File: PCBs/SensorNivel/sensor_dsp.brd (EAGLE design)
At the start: 100 x 80 mm, 76 parts, among them IC1 LD117AS, IC2 DSPIC33FJ12GP202/SP, IC4 7805TV, IC5 ICL7660CPA, IC6 4069N, IC7 LM324N, IC8 LM324N, IC9 MAX481CPA

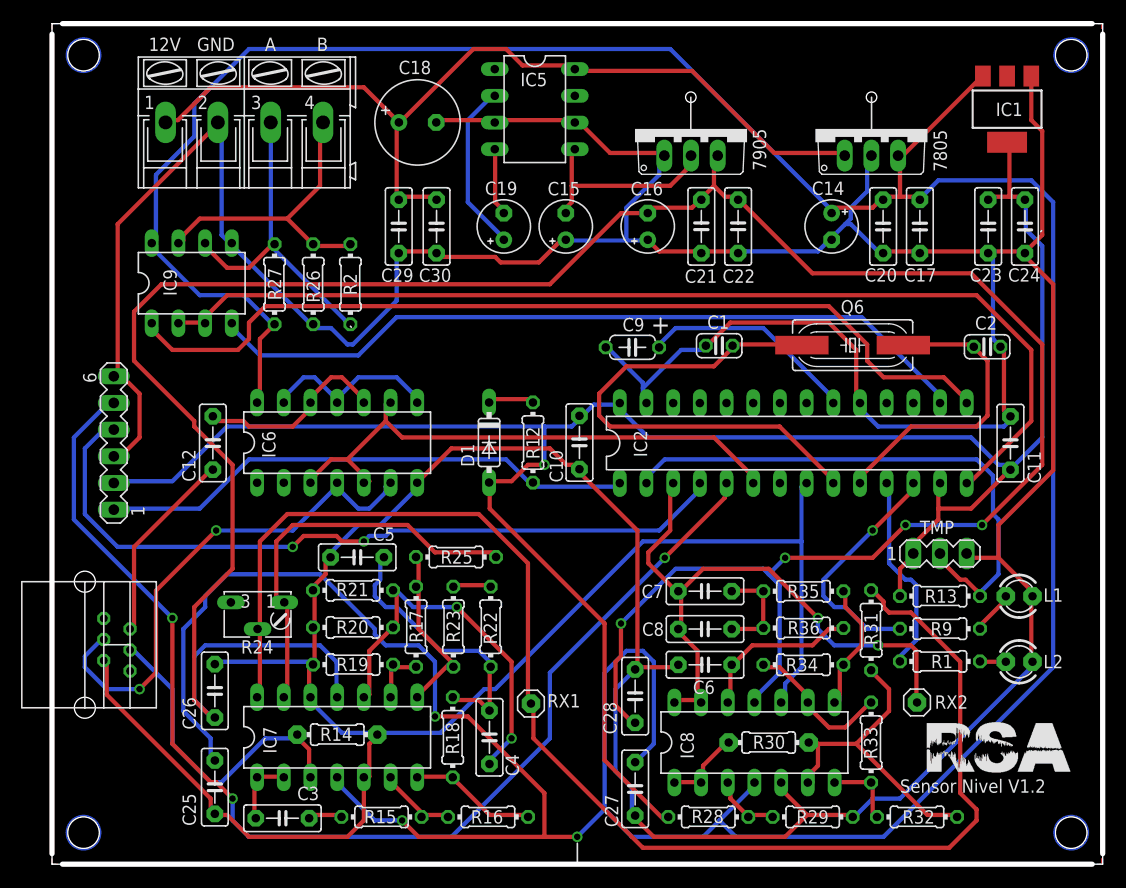
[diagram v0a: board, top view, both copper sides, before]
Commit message: Se rediseñaron y corrigieron los diseños de los PCB. Se diseñaron las platinas de los vertederos basadas en las medidas de los soportes.
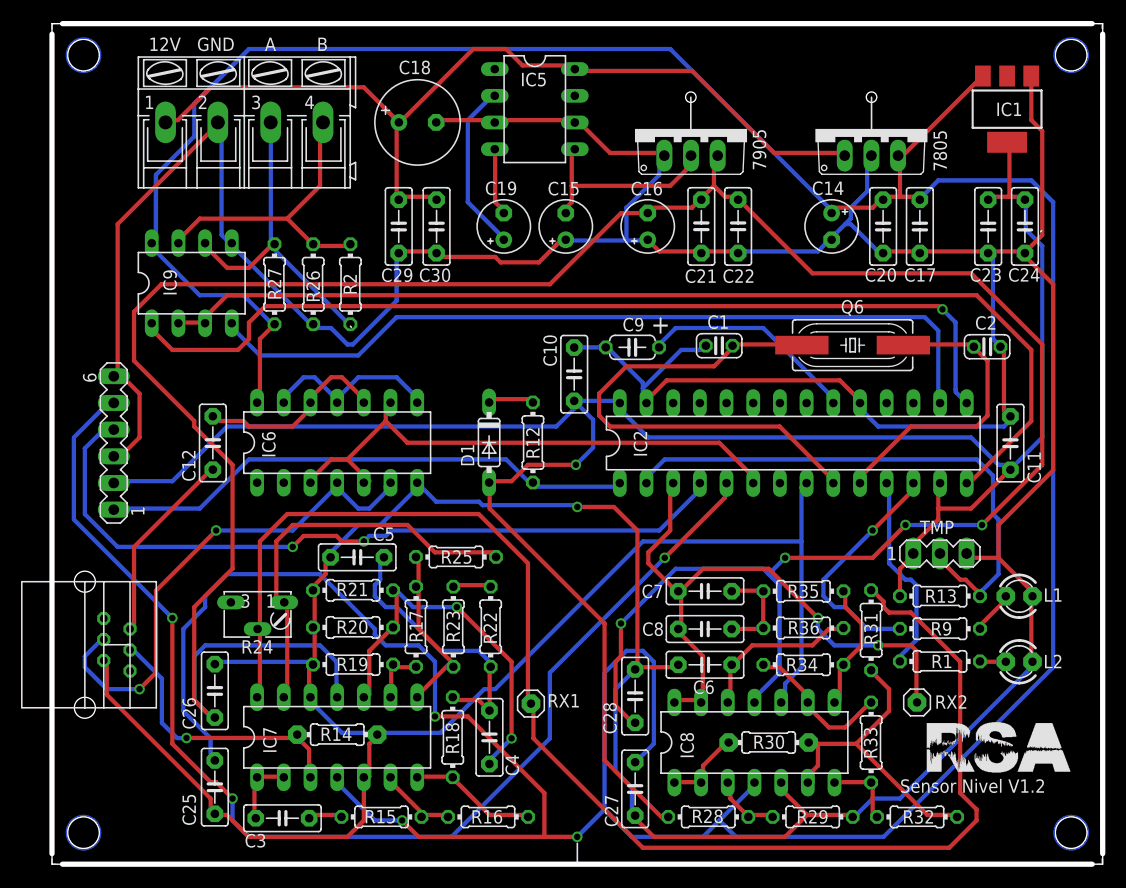
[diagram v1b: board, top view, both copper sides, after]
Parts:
- moved C10 6.52 mm to (49.7, 46.6), turned to 270 degrees
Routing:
- net VDD: track 198.1 -> 205.5 mm
- net R+: track 30.6 -> 26.6 mm, vias 0 -> 1
- net ERX: track 74.2 -> 77.7 mm
- net ETX: track 86.4 -> 89.3 mm, vias 0 -> 1
- net AGND: track 582.6 -> 583.8 mm, vias 0 -> 1
- net ADC_IN: track 59.0 -> 59.7 mm

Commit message: Se hicieron modificaciones al Firmware y al Software. Version funcional.
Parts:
- C1, C2: value (none) -> 22pF
- C10, C11, C12, C25, C26, C27, C28: value (none) -> 100nF
- C3, C4, C5: value (none) -> 10nF
- C6, C7, C8: value (none) -> 1nF
- C9: value (none) -> 10uF
- Q6: value (none) -> 8MHz
- R12, R13: value (none) -> 4.7K
- R14, R15, R20, R28, R29, R30, R31, R32, R33, R34: value (none) -> 10K
- R16: value (none) -> 1M
- R17, R25: value (none) -> 1K
- R18, R26, R27: value (none) -> 3.3K
- R19: value (none) -> 470
- R2: value (none) -> 120
- R21: value (none) -> 390
- R22, R23: value (none) -> 220
- R35, R36: value (none) -> 2.2K
